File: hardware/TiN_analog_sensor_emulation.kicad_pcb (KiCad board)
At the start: 2 copper layers, 100 x 100 mm, 141 parts, among them J1 Micro_SD_Card, J2 BOOT0, J3 Conn_01x04_Male, J4 Barrel_Jack, J5 Conn_01x03_Male, J6 display, SW1 SW_right, SW2 SW_right, SW3 SW_top, SW4 SW_middle, SW5 SW_bot, SW6 SW_Left, SW7 SW_middle2, U1 STM32F042C6Tx, U10 MCP42010, U11 ADA4898-3, U12 ADA4898-3, U13 MCP42010, U14 MCP42010, U15 MCP42050, U16 MCP42050, U17 MCP42050, U18 LT1528CQ, U19 LT1529CQ#PBF, U2 ADA4898-3, U3 ADA4898-3, U4 MCP42010, U5 ADA4898-3, U6 ADA4898-3, U7 MCP42010, U8 ADA4898-3, U9 ADA4898-3

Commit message: update pinoutu, zmiany footprintów
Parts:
- removed JP1: Jumper_NO_Small, Jumper:SolderJumper-2_P1.3mm_Open_TrianglePad1.0x1.5mm
- J1: footprint Connector_Card:microSD_HC_Hirose_DM3AT-SF-PEJM5 -> symbols:MOLEX_503398-1892
- R22: value 15 -> N.C
- moved C27 124.4 mm to (174.9, 130.1), turned to 270 degrees
- moved C28 112.7 mm to (185.7, 141.7), turned to 270 degrees
- moved C12 110.4 mm to (185.7, 130.0), turned to 270 degrees
- moved C23 108.6 mm to (175.3, 116.8), turned to 270 degrees
- moved C49 102.3 mm to (214.9, 95.6)
- moved C42 97.2 mm to (174.9, 141.9), turned to 270 degrees
- moved C37 97.2 mm to (219.9, 96.0)
- moved C55 93.6 mm to (213.9, 87.9)
- moved C26 93.3 mm to (185.9, 106.4), turned to 270 degrees
- moved C19 89.9 mm to (220.9, 89.9)
- moved C24 87.0 mm to (175.2, 106.7), turned to 270 degrees
- moved C56 86.1 mm to (226.2, 77.0)
- moved C48 86.0 mm to (231.6, 72.9)
- moved C39 85.8 mm to (186.0, 116.7), turned to 270 degrees
- moved C45 85.7 mm to (219.7, 83.2)
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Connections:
- D2 pad 1: Net-(D2-Pad1) -> +9V
- J4 pad 2: Net-(D2-Pad1) -> Net-(J4-Pad2)
- JP2 pad 2: Net-(JP1-Pad1) -> Net-(JP2-Pad2)
- R22 pad 2: Net-(JP1-Pad2) -> Net-(JP2-Pad2)
- R23 pad 1: Net-(JP1-Pad1) -> Net-(JP2-Pad2)
- TH1 pad 2: Net-(D2-Pad1) -> Net-(J4-Pad2)
- U18 pad 2: Net-(JP1-Pad1) -> Net-(JP2-Pad2)

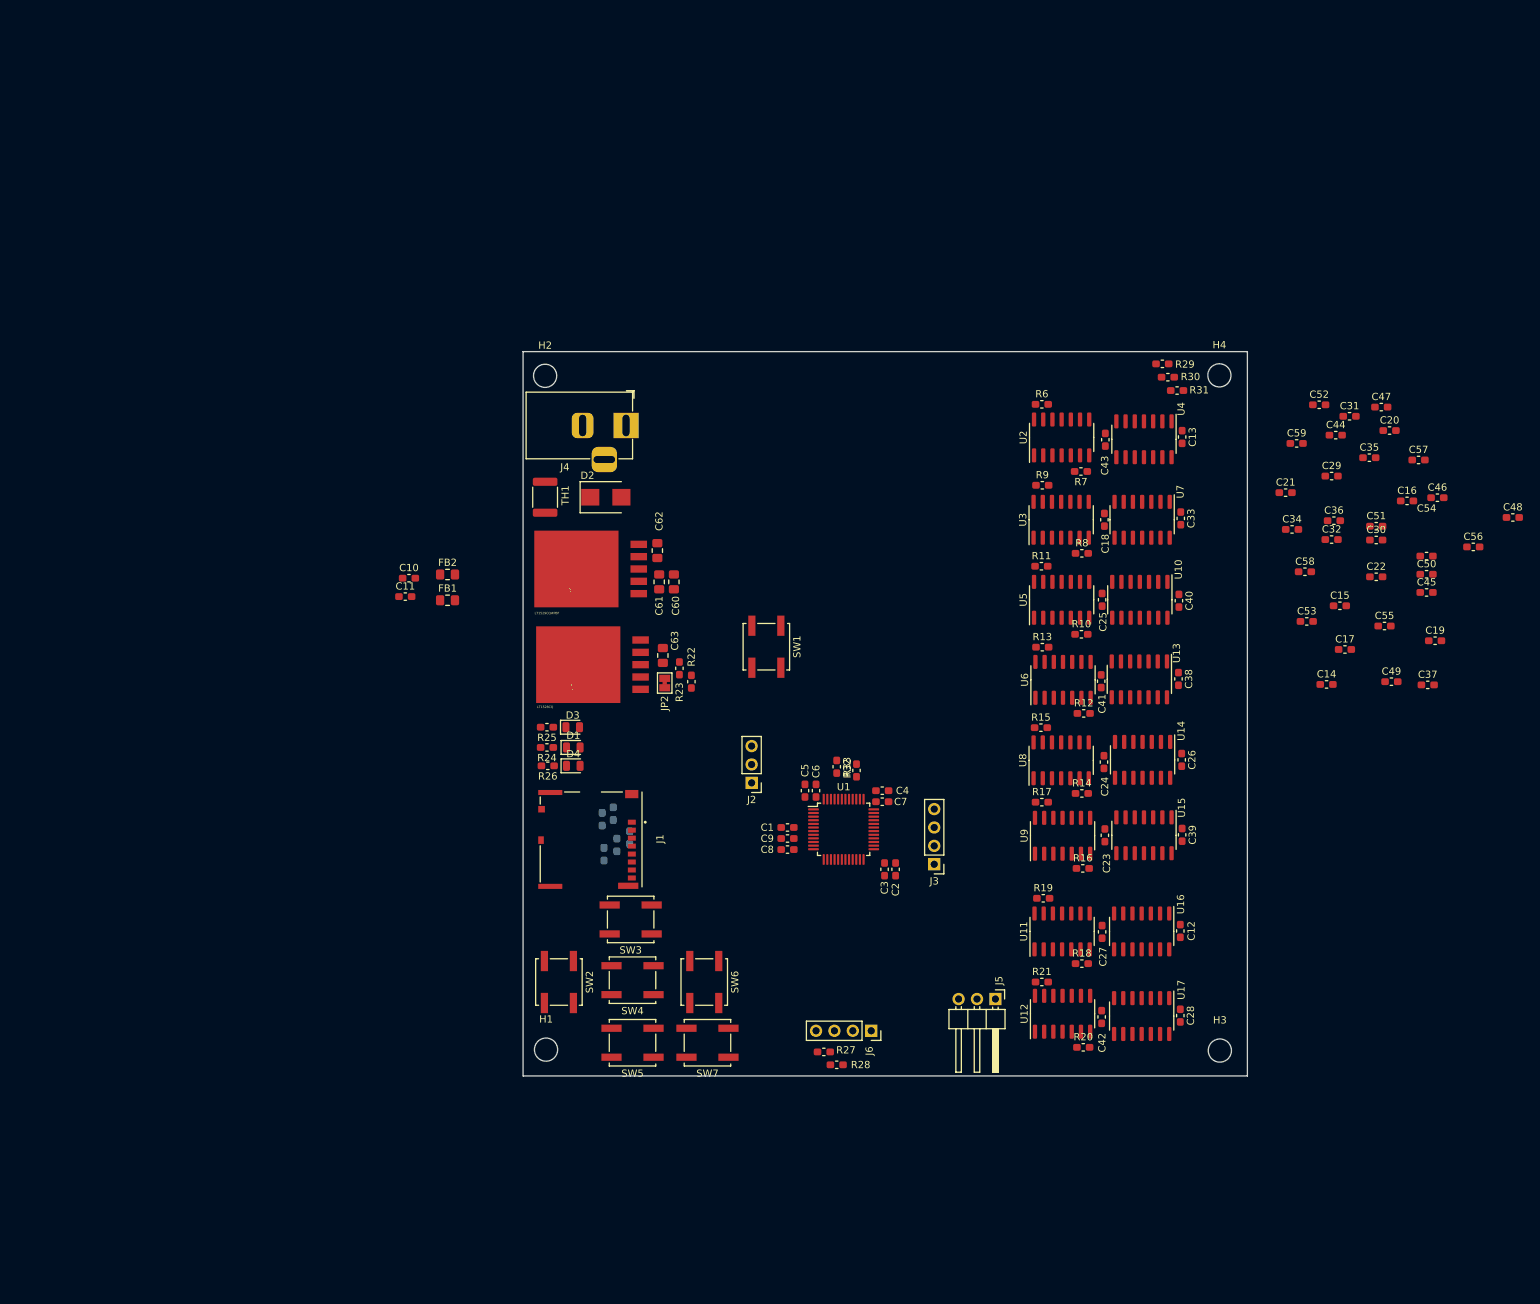
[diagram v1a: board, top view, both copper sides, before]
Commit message: dodanie zabezpieczen portów i dzialniki napiec na wejsciach adc
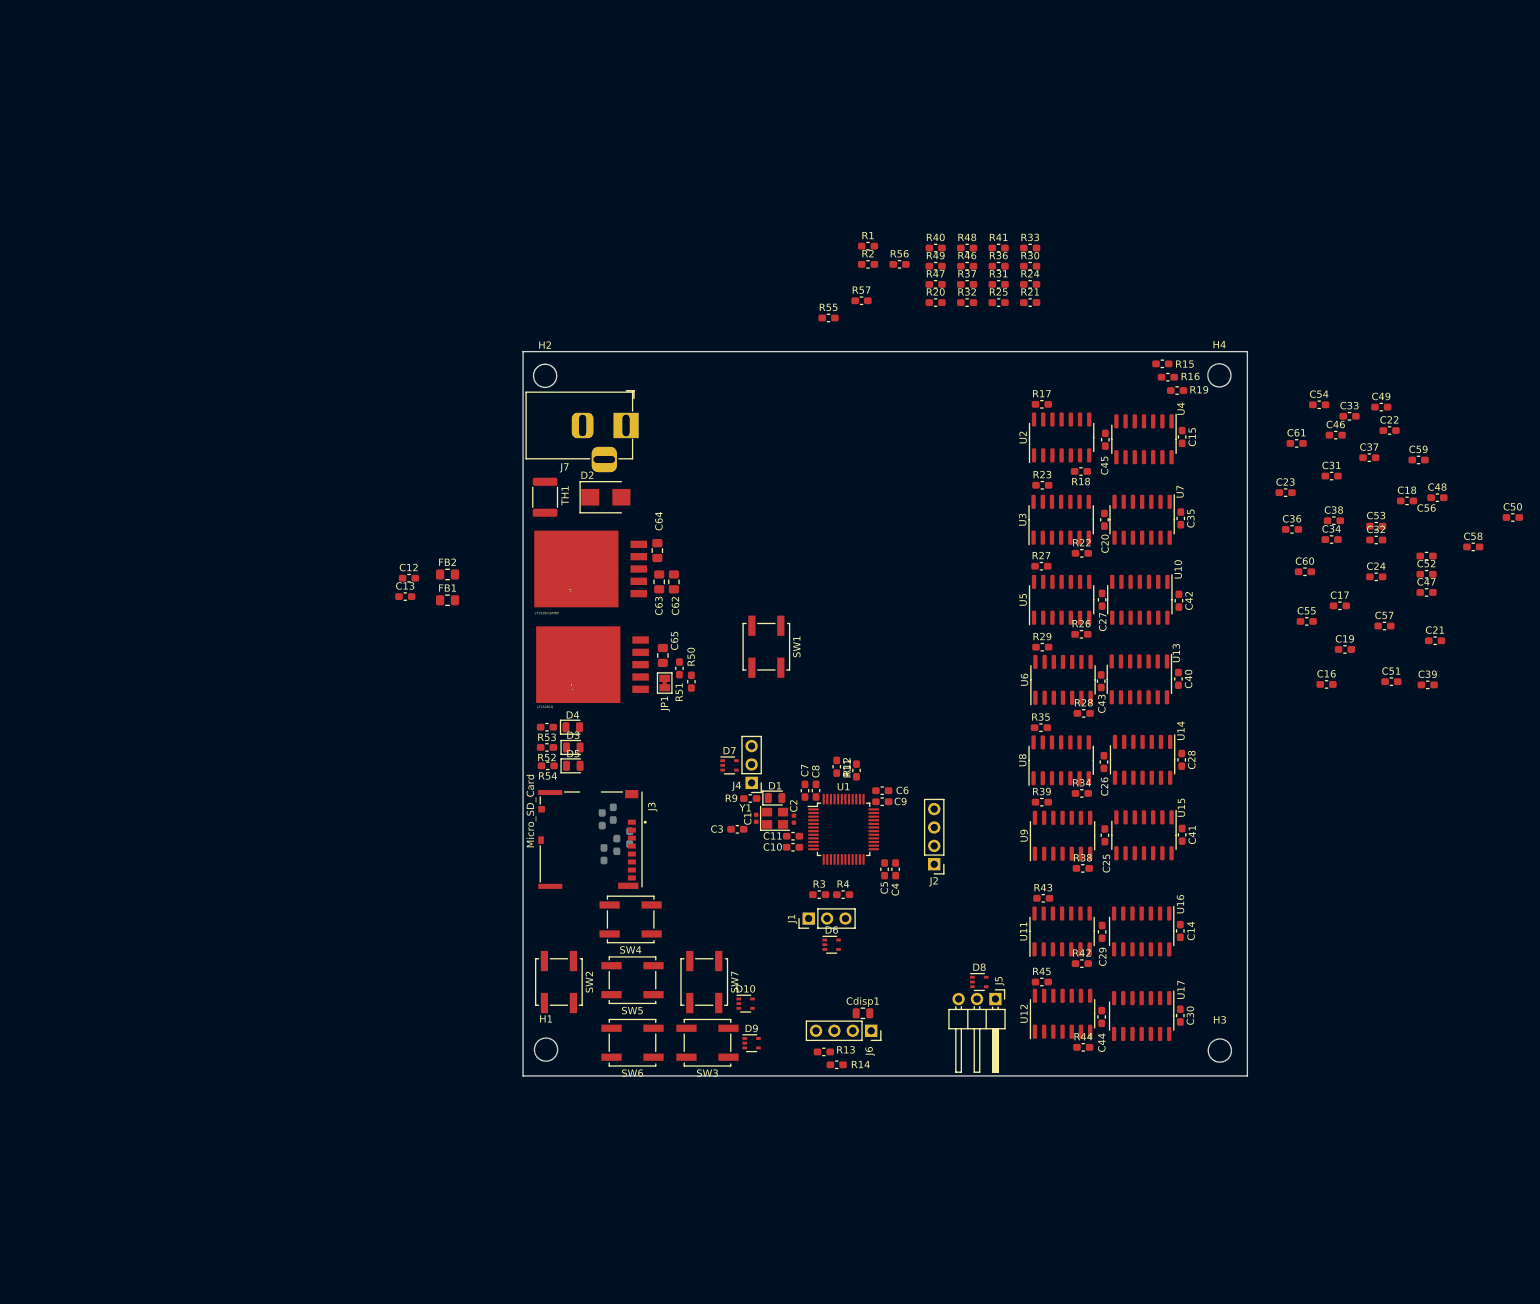
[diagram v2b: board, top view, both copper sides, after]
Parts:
- added C1: 22p, Capacitor_SMD:C_0402_1005Metric, F.Cu at (127.2, 114.4)
- added C2: 22p, Capacitor_SMD:C_0402_1005Metric, F.Cu at (132.4, 114.6)
- added Cdisp1: 10u, Capacitor_SMD:C_0805_2012Metric, F.Cu at (141.9, 141.4)
- added D1: RED, LED_SMD:LED_0805_2012Metric, F.Cu at (129.8, 111.6)
- added D10: PESD5V0L4UG, Package_TO_SOT_SMD:SOT-353_SC-70-5, F.Cu at (125.7, 140.0)
- added D6: PESD5V0L4UG, Package_TO_SOT_SMD:SOT-353_SC-70-5, F.Cu at (137.6, 131.9)
- added D7: PESD5V0L4UG, Package_TO_SOT_SMD:SOT-353_SC-70-5, F.Cu at (123.5, 107.1)
- added D8: PESD5V0L4UG, Package_TO_SOT_SMD:SOT-353_SC-70-5, F.Cu at (158.0, 137.0)
- added D9: PESD5V0L4UG, Package_TO_SOT_SMD:SOT-353_SC-70-5, F.Cu at (126.6, 145.5)
- added J1: ADc, Connector_PinHeader_2.54mm:PinHeader_1x03_P2.54mm_Vertical, F.Cu at (134.4, 128.3)
- added R1: 220k, Resistor_SMD:R_0603_1608Metric_Pad1.05x0.95mm_HandSolder, F.Cu at (142.6, 35.4)
- added R2: 330k, Resistor_SMD:R_0603_1608Metric_Pad1.05x0.95mm_HandSolder, F.Cu at (142.6, 38.0)
- added R20: 220k, Resistor_SMD:R_0603_1608Metric_Pad1.05x0.95mm_HandSolder, F.Cu at (152.0, 43.2)
- added R21: 330k, Resistor_SMD:R_0603_1608Metric_Pad1.05x0.95mm_HandSolder, F.Cu at (165.0, 43.2)
- added R24: 220k, Resistor_SMD:R_0603_1608Metric_Pad1.05x0.95mm_HandSolder, F.Cu at (165.0, 40.7)
- added R25: 330k, Resistor_SMD:R_0603_1608Metric_Pad1.05x0.95mm_HandSolder, F.Cu at (160.7, 43.2)
- added R3: 220k, Resistor_SMD:R_0603_1608Metric_Pad1.05x0.95mm_HandSolder, F.Cu at (135.9, 125.0)
- added R30: 220k, Resistor_SMD:R_0603_1608Metric_Pad1.05x0.95mm_HandSolder, F.Cu at (165.0, 38.2)
- added R31: 330k, Resistor_SMD:R_0603_1608Metric_Pad1.05x0.95mm_HandSolder, F.Cu at (160.7, 40.7)
- added R32: 220k, Resistor_SMD:R_0603_1608Metric_Pad1.05x0.95mm_HandSolder, F.Cu at (156.3, 43.2)
- added R33: 330k, Resistor_SMD:R_0603_1608Metric_Pad1.05x0.95mm_HandSolder, F.Cu at (165.0, 35.7)
- added R36: 220k, Resistor_SMD:R_0603_1608Metric_Pad1.05x0.95mm_HandSolder, F.Cu at (160.7, 38.2)
- added R37: 330k, Resistor_SMD:R_0603_1608Metric_Pad1.05x0.95mm_HandSolder, F.Cu at (156.3, 40.7)
- added R4: 330k, Resistor_SMD:R_0603_1608Metric_Pad1.05x0.95mm_HandSolder, F.Cu at (139.2, 125.0)
- added R40: 220k, Resistor_SMD:R_0603_1608Metric_Pad1.05x0.95mm_HandSolder, F.Cu at (152.0, 35.7)
- added R41: 330k, Resistor_SMD:R_0603_1608Metric_Pad1.05x0.95mm_HandSolder, F.Cu at (160.7, 35.7)
- added R46: 220k, Resistor_SMD:R_0603_1608Metric_Pad1.05x0.95mm_HandSolder, F.Cu at (156.3, 38.2)
- added R47: 330k, Resistor_SMD:R_0603_1608Metric_Pad1.05x0.95mm_HandSolder, F.Cu at (152.0, 40.7)
- added R48: 220k, Resistor_SMD:R_0603_1608Metric_Pad1.05x0.95mm_HandSolder, F.Cu at (156.3, 35.7)
- added R49: 330k, Resistor_SMD:R_0603_1608Metric_Pad1.05x0.95mm_HandSolder, F.Cu at (152.0, 38.2)
- added R55: 22, Resistor_SMD:R_0603_1608Metric_Pad1.05x0.95mm_HandSolder, F.Cu at (137.2, 45.4)
- added R56: 22, Resistor_SMD:R_0603_1608Metric_Pad1.05x0.95mm_HandSolder, F.Cu at (147.0, 38.0)
- added R57: 22, Resistor_SMD:R_0603_1608Metric_Pad1.05x0.95mm_HandSolder, F.Cu at (141.7, 43.0)
- added R9: 220, Resistor_SMD:R_0603_1608Metric_Pad1.05x0.95mm_HandSolder, F.Cu at (126.4, 111.7)
- added Y1: Crystal_GND24, Crystal:Crystal_SMD_3225-4Pin_3.2x2.5mm, F.Cu at (129.8, 114.4)
- moved C3 6.93 mm to (124.6, 116.0)
- moved C10 0.83 mm to (132.3, 118.4)
- moved C11 0.83 mm to (132.3, 116.9)
- renumbered C8 to C10, C9 to C11, C10 to C12, C11 to C13, C12 to C14, C13 to C15, C14 to C16, C15 to C17, C16 to C18, C17 to C19, C18 to C20, C19 to C21, C20 to C22, C21 to C23, C22 to C24, C23 to C25, C24 to C26, C25 to C27, C26 to C28, C27 to C29, C1 to C3, C28 to C30, C29 to C31, C30 to C32, C31 to C33, C32 to C34, C33 to C35, C34 to C36, C35 to C37, C36 to C38, C37 to C39, C2 to C4, C38 to C40, C39 to C41, C40 to C42, C41 to C43, C42 to C44, C43 to C45, C44 to C46, C45 to C47, C46 to C48, C47 to C49, C3 to C5, C48 to C50, C49 to C51, C50 to C52, C51 to C53, C52 to C54, C53 to C55, C54 to C56, C55 to C57, C56 to C58, C57 to C59, C4 to C6, C58 to C60, C59 to C61, C60 to C62, C61 to C63, C62 to C64, C63 to C65, C5 to C7, C6 to C8, C7 to C9, D1 to D3, D3 to D4, D4 to D5, J3 to J2, J1 to J3, J2 to J4, J4 to J7, JP2 to JP1, R5 to R10, R32 to R11, R33 to R12, R27 to R13, R28 to R14, R29 to R15, R30 to R16, R6 to R17, R7 to R18, R31 to R19, R8 to R22, R9 to R23, R10 to R26, R11 to R27, R12 to R28, R13 to R29, R14 to R34, R15 to R35, R16 to R38, R17 to R39, R18 to R42, R19 to R43, R20 to R44, R21 to R45, R1 to R5, R22 to R50, R23 to R51, R24 to R52, R25 to R53, R26 to R54, R2 to R6, R3 to R7, R4 to R8, SW7 to SW3, SW3 to SW4, SW4 to SW5, SW5 to SW6, SW6 to SW7, U19 to U18, U18 to U19
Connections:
- C3 pad 1: GND -> /MCU/~RST
- C3 pad 2: /MCU/~RST -> GND
- J5 pad 1: /MCU/USART_CK -> Net-(D8-Pad1)
- J5 pad 2: /MCU/USART_TX -> Net-(D8-Pad3)
- J5 pad 3: /MCU/USART_RX -> Net-(D8-Pad4)
- U1 pad 18: /MCU/sw_bot -> /MCU/ADC8
- U1 pad 19: /MCU/sw_right -> /MCU/ADC9
- U1 pad 2: (no net) -> /MCU/sw_right
- U1 pad 3: (no net) -> /MCU/sw_bot
- U1 pad 4: (no net) -> /MCU/led_signal
- U1 pad 5: (no net) -> Net-(C1-Pad1)
- U1 pad 6: (no net) -> Net-(C2-Pad2)
- U11 pad 8: /MCU/ADC6 -> Net-(R46-Pad1)
- U11 pad 9: /MCU/ADC6 -> Net-(R46-Pad1)
- U12 pad 8: /MCU/ADC7 -> Net-(R48-Pad1)
- U12 pad 9: /MCU/ADC7 -> Net-(R48-Pad1)
- U2 pad 8: /MCU/ADC0 -> Net-(R20-Pad1)
- U2 pad 9: /MCU/ADC0 -> Net-(R20-Pad1)
- U3 pad 8: /MCU/ADC1 -> Net-(R24-Pad1)
- U3 pad 9: /MCU/ADC1 -> Net-(R24-Pad1)
- U5 pad 8: /MCU/ADC2 -> Net-(R30-Pad1)
- U5 pad 9: /MCU/ADC2 -> Net-(R30-Pad1)
- U6 pad 8: /MCU/ADC3 -> Net-(R32-Pad1)
- U6 pad 9: /MCU/ADC3 -> Net-(R32-Pad1)
- U8 pad 8: /MCU/ADC4 -> Net-(R36-Pad1)
- U8 pad 9: /MCU/ADC4 -> Net-(R36-Pad1)
- U9 pad 8: /MCU/ADC5 -> Net-(R40-Pad1)
- U9 pad 9: /MCU/ADC5 -> Net-(R40-Pad1)

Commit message: mała poprawka przy kondensatorach od opampow
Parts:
- moved R56 149.3 mm to (65.7, 163.2), turned to 90 degrees
- moved R57 146.3 mm to (60.7, 164.8), turned to 90 degrees
- moved R1 145.3 mm to (42.0, 140.2)
- moved R2 141.2 mm to (45.2, 140.2)
- moved R55 139.1 mm to (63.1, 163.1), turned to 90 degrees
- moved D8 93.6 mm to (68.5, 164.3)
- moved J5 93.6 mm to (70.7, 166.6)
- moved C2 91.7 mm to (41.7, 128.4)
- moved C4 91.7 mm to (55.8, 135.3)
- moved C5 91.7 mm to (54.2, 135.3)
- moved C7 91.7 mm to (44.8, 124.5)
- moved C8 91.7 mm to (43.2, 124.5)
- moved D1 91.7 mm to (39.1, 125.5)
- moved U1 91.7 mm to (48.6, 129.8)
- moved Y1 91.7 mm to (39.1, 128.3)
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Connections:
- C17 pad 2: GNDA -> +5V
- C19 pad 2: GNDA -> +5V
- C22 pad 1: GNDA -> +5V
- C24 pad 1: GNDA -> +5V
- C32 pad 2: GNDA -> +5V
- C34 pad 2: GNDA -> +5V
- C37 pad 1: GNDA -> +5V
- C39 pad 1: GNDA -> +5V
- C47 pad 2: GNDA -> +5V
- C49 pad 2: GNDA -> +5V
- C51 pad 1: GNDA -> +5V
- C53 pad 1: GNDA -> +5V
- C55 pad 2: GNDA -> +5V
- C57 pad 2: GNDA -> +5V
- C59 pad 1: GNDA -> +5V
- C61 pad 1: GNDA -> +5V

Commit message: trwa układanie, dodane złacze golpin
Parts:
- added J8: Conn_02x08_Odd_Even, Connector_PinHeader_2.54mm:PinHeader_2x08_P2.54mm_Vertical, F.Cu at (130.9, 58.2)
- C16, C17, C18, C24, C32, C33, C38, C39, C47, C49, C51, C52, C56, C58, C59, C60, D8, R20, R21, R24, R25, R30, R31, R32, R33, R36, R37, R40, R41, R46, R47, R48, R49: moved to B.Cu
- R10, R5, R6, R7, R8: moved to F.Cu
- moved C60 88.4 mm to (167.7, 55.9)
- moved C16 83.9 mm to (165.7, 144.8), turned to 180 degrees
- moved R57 83.3 mm to (139.0, 136.4), turned to 270 degrees
- moved C56 76.4 mm to (165.8, 65.3), turned to 180 degrees
- moved R55 75.8 mm to (134.0, 136.2)
- moved R56 75.6 mm to (136.4, 136.5)
- moved C17 74.6 mm to (165.9, 133.5)
- moved J5 73.3 mm to (139.0, 140.0)
- moved D8 71.2 mm to (136.3, 143.0), turned to 180 degrees
- moved C58 65.5 mm to (167.8, 67.2)
- moved C18 64.2 mm to (167.8, 135.4), turned to 180 degrees
- moved R21 57.5 mm to (149.0, 71.6), turned to 270 degrees
- moved R25 54.7 mm to (146.4, 71.6), turned to 270 degrees
- moved C59 53.7 mm to (166.0, 76.6), turned to 180 degrees
- moved R20 53.4 mm to (149.1, 67.5), turned to 270 degrees
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- renumbered SW1 to SW_rst1
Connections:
- net Net-(R20-Pad1) renamed /digital_pot/pot1
- net Net-(R24-Pad1) renamed /digital_pot/pot2
- net Net-(R30-Pad1) renamed /digital_pot/pot3
- net Net-(R32-Pad1) renamed /digital_pot/pot4
- net Net-(R36-Pad1) renamed /digital_pot/pot5
- net Net-(R40-Pad1) renamed /digital_pot/pot6
- net Net-(R46-Pad1) renamed /digital_pot/pot7
- net Net-(R48-Pad1) renamed /digital_pot/pot8
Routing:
- net +5V: track 0.00 -> 264.1 mm, vias 0 -> 32
- net /MCU/POTSCK: track 0.00 -> 157.6 mm
- net /digital_pot/pot8: track 0.00 -> 124.5 mm
- net /digital_pot/pot7: track 0.00 -> 110.0 mm
- net /digital_pot/pot6: track 0.00 -> 96.5 mm
- net /digital_pot/CS: track 0.00 -> 94.6 mm, vias 0 -> 8
- net /MCU/POTSHDN: track 0.00 -> 92.2 mm, vias 0 -> 8
- net /MCU/POTRST: track 0.00 -> 91.7 mm, vias 0 -> 8
- net /digital_pot/pot5: track 0.00 -> 82.5 mm
- net /digital_pot/pot4: track 0.00 -> 69.2 mm
- net +9V: track 0.00 -> 58.4 mm
- net /digital_pot/pot3: track 0.00 -> 57.0 mm
- net /digital_pot/pot2: track 0.00 -> 44.1 mm
- net +3V3: track 0.00 -> 32.4 mm, vias 0 -> 2
- net /digital_pot/pot1: track 0.00 -> 32.0 mm
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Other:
- net class Default: clearance 0.2 -> 0.25; trace_width 0.25 -> 0.2
- net class power added: clearance 0.4, trace_width 0.5, via_dia 0.8, via_drill 0.4
- rule trace_clearance: 0.2 -> 0.25
